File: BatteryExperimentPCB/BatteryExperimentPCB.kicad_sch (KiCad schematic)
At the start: 32 parts, among them J1 USB_C_Receptacle_USB2.0_14P, J2 Conn_01x11_Pin, J3 Conn_01x11_Pin, Q1 DMG1012T, SW1 SW_Push, U1 ATtiny3226-M, U2 USBLC6-2P6, U3 BQ25628RYKR

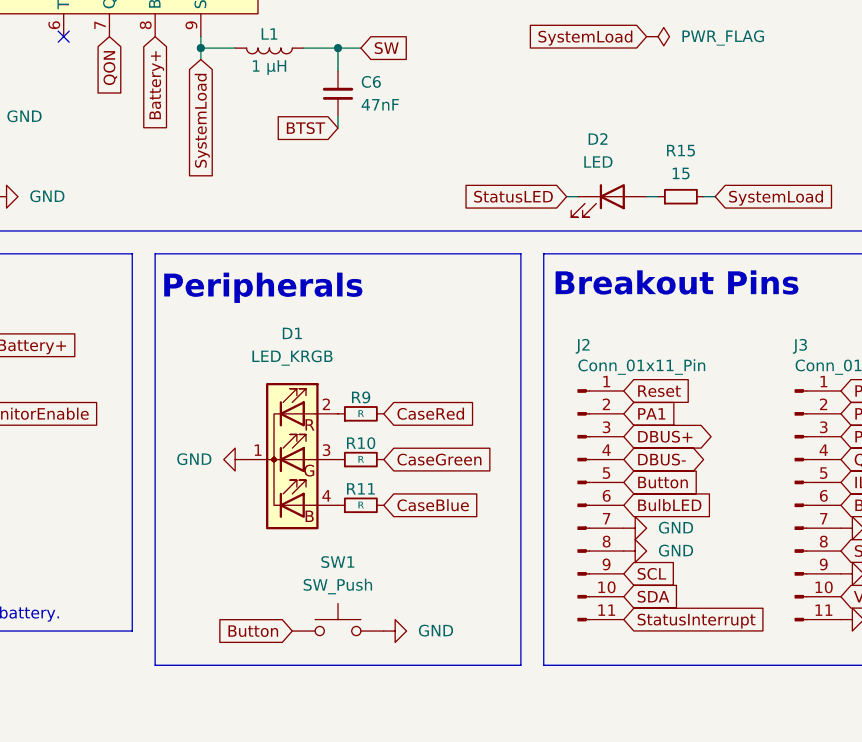
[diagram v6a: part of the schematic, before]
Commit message: updating data sheet for rgb led, adding more resistor values
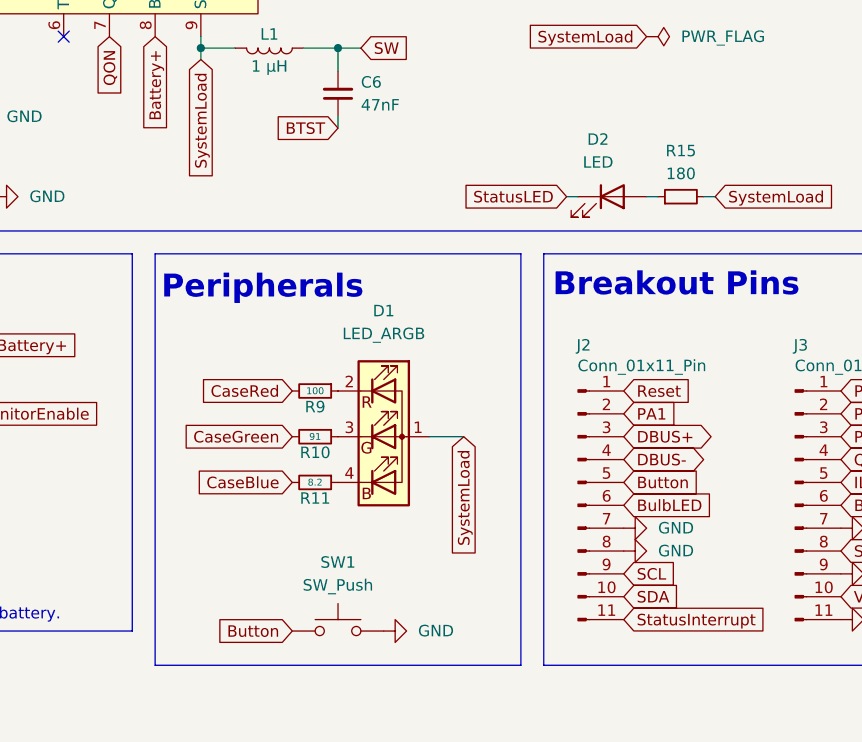
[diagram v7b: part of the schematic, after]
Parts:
- removed D1: LED_KRGB, symbol Device:LED_KRGB
- added D1: LED_ARGB, symbol Device:LED_ARGB
- R10: value R -> 91
- R11: value R -> 8.2
- R15: value 15 -> 180
- R9: value R -> 100
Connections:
- net SystemLoad: now also D1.1 (A)
- net at R9.1: now also D1.2 (RK)
- net at R10.1: now also D1.3 (GK)
- net at R11.1: now also D1.4 (BK)
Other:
- moved on the sheet: R10, R11, R9

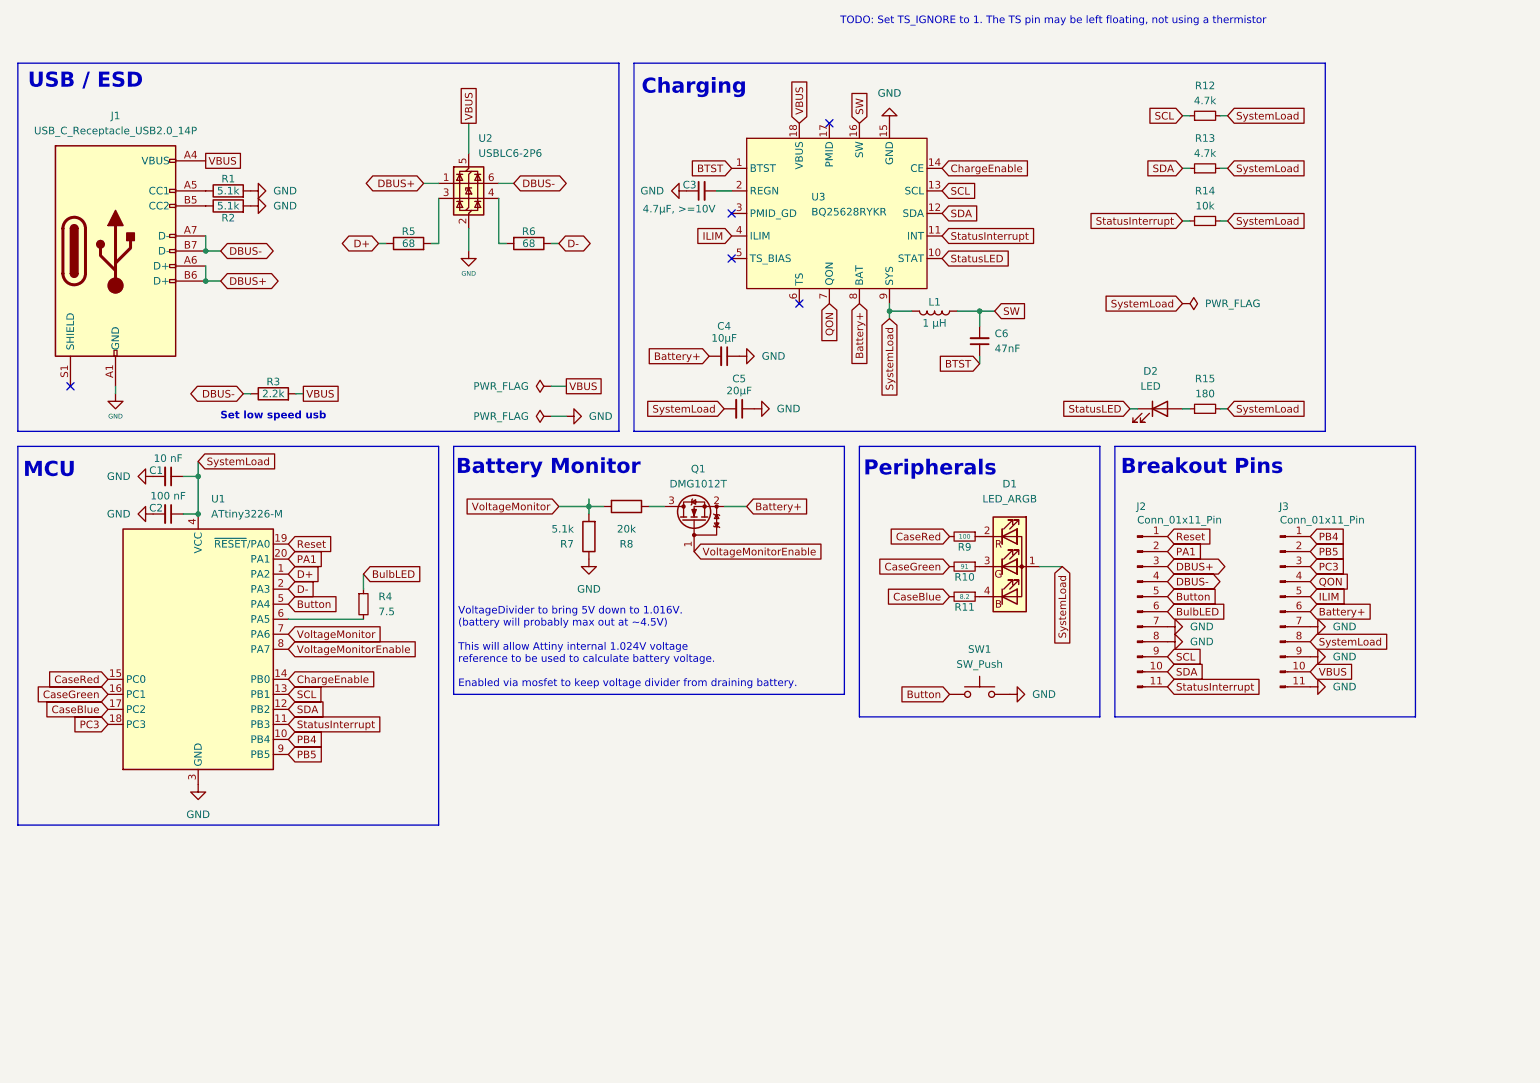
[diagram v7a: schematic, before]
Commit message: changed SystemLoad label to +3.75V power label
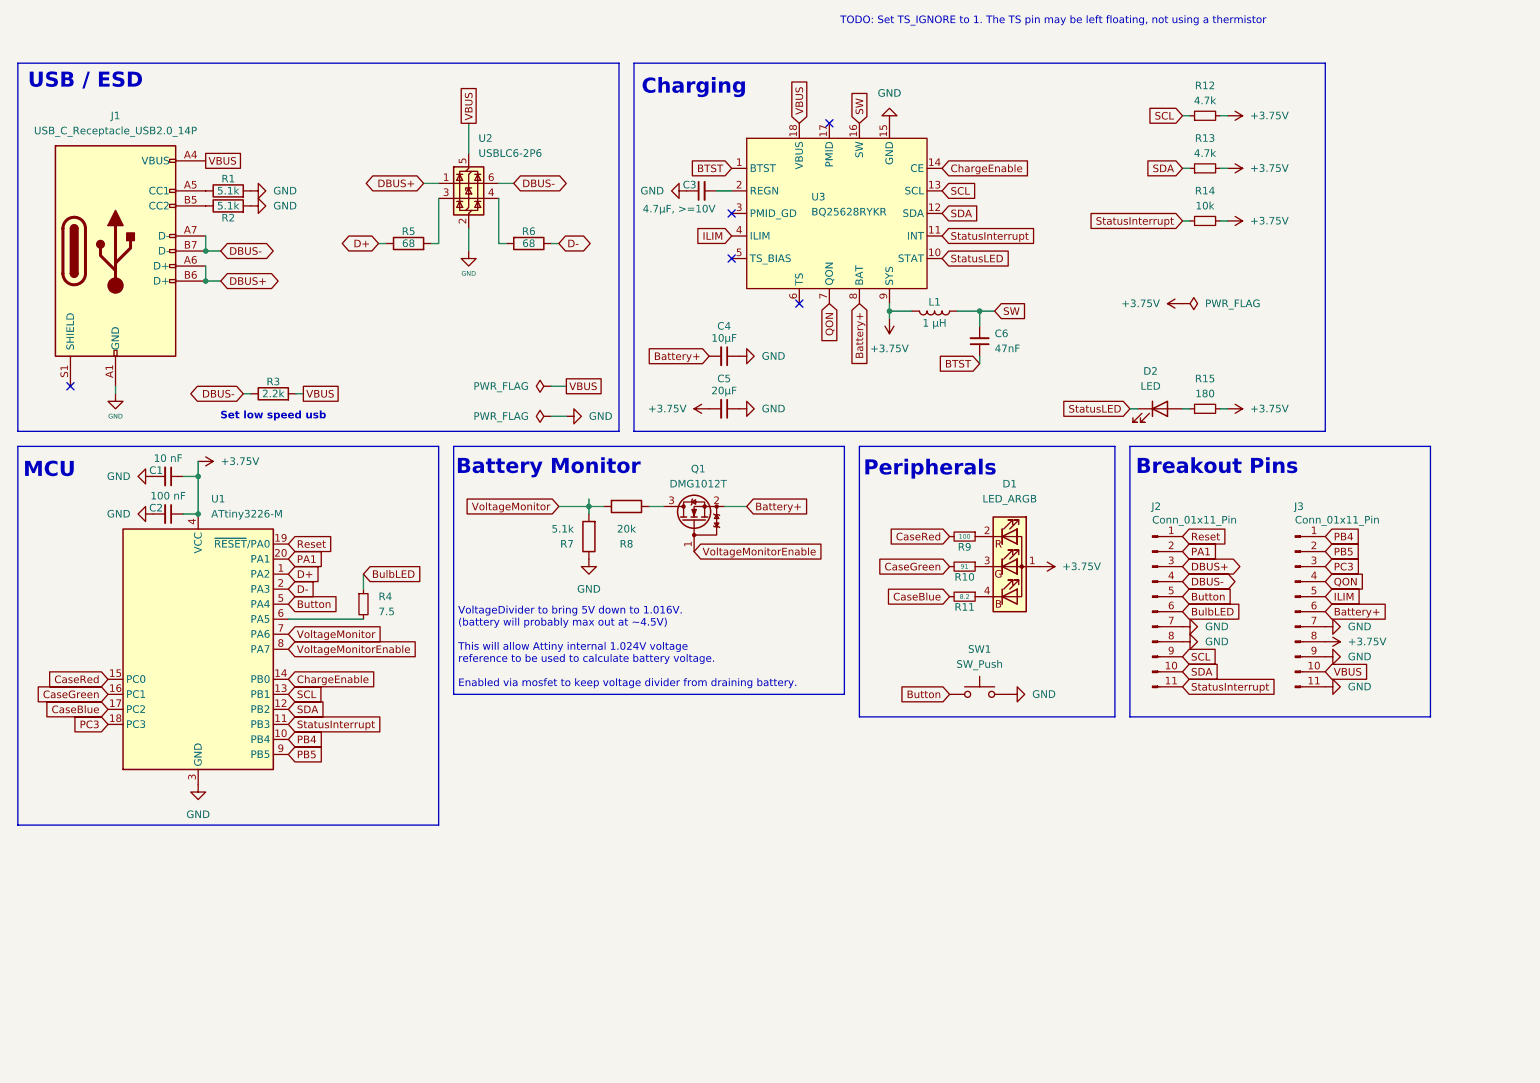
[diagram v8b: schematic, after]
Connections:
- net SystemLoad renamed +3.75V
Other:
- moved on the sheet: C5, J2, J3
